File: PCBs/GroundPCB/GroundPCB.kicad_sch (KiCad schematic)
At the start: 42 parts, among them IC1 SWITCH-HSWA4-63DR+, IC2 SWITCH-HSWA4-63DR+, J1 SMA-LPRS-CONNECTOR, J2 Conn_02x03_Odd_Even, U1 HMC452ST89ETR, U2 PGA-103+, U3 RFM96W-433S2, U4 DS3231M

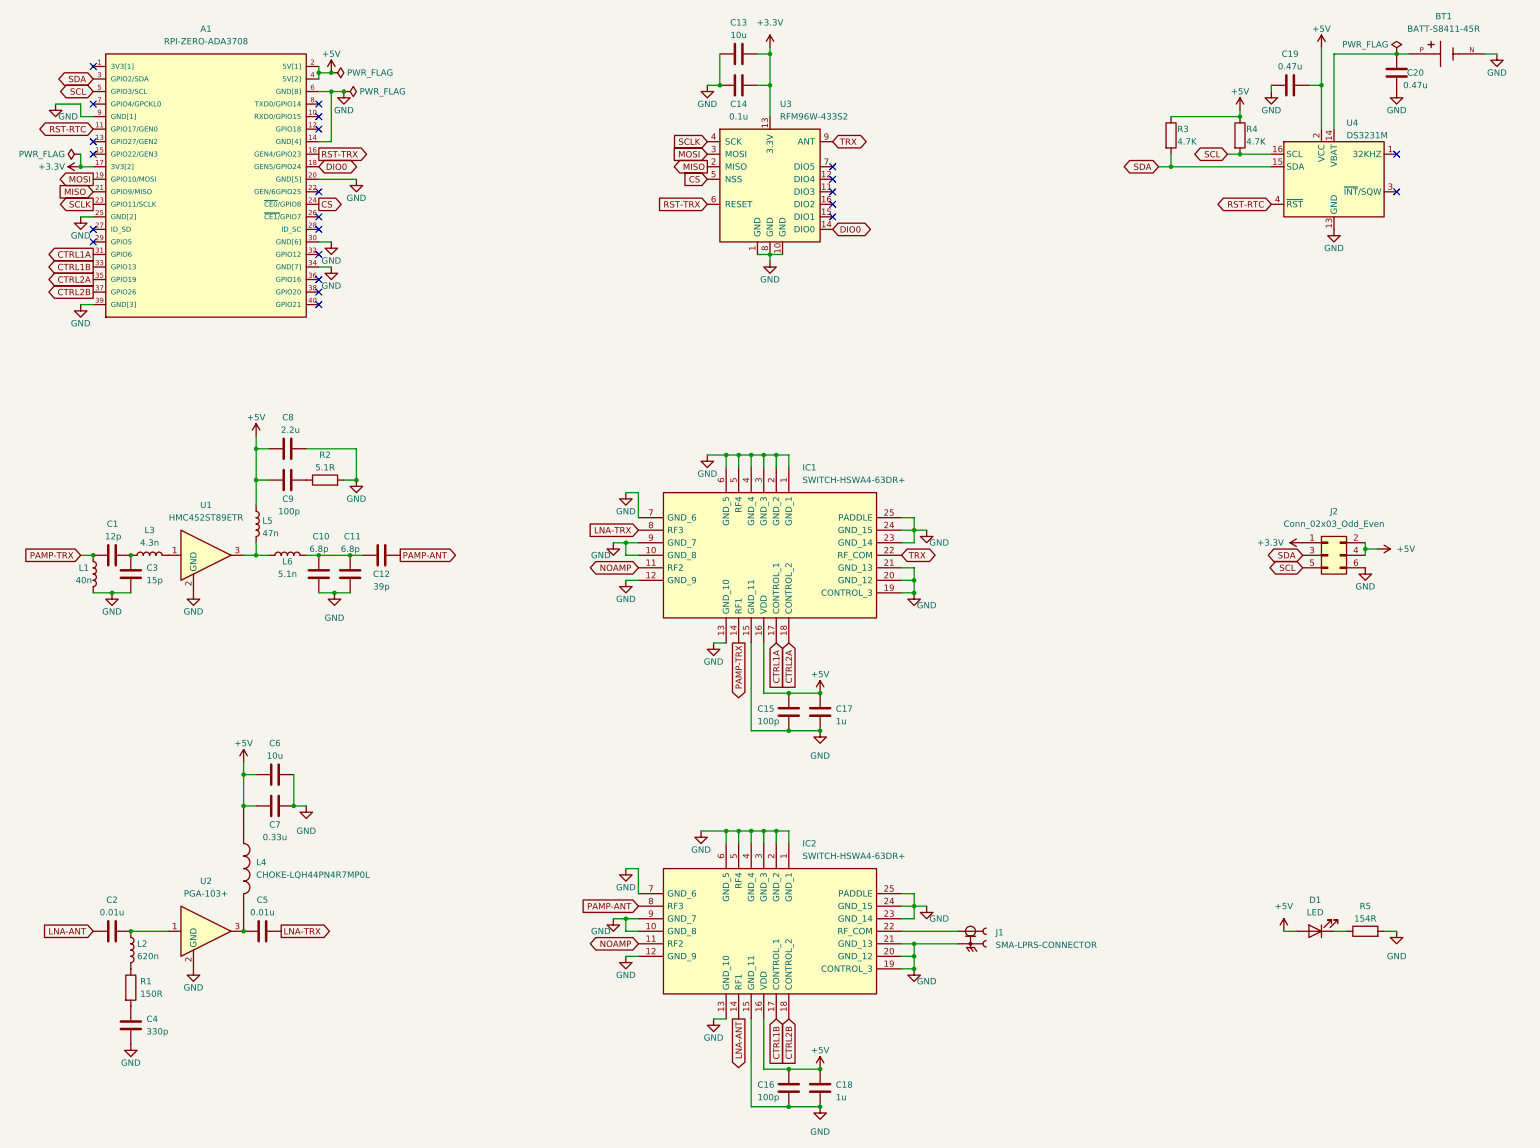
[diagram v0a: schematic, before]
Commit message: connectors, switch, test points
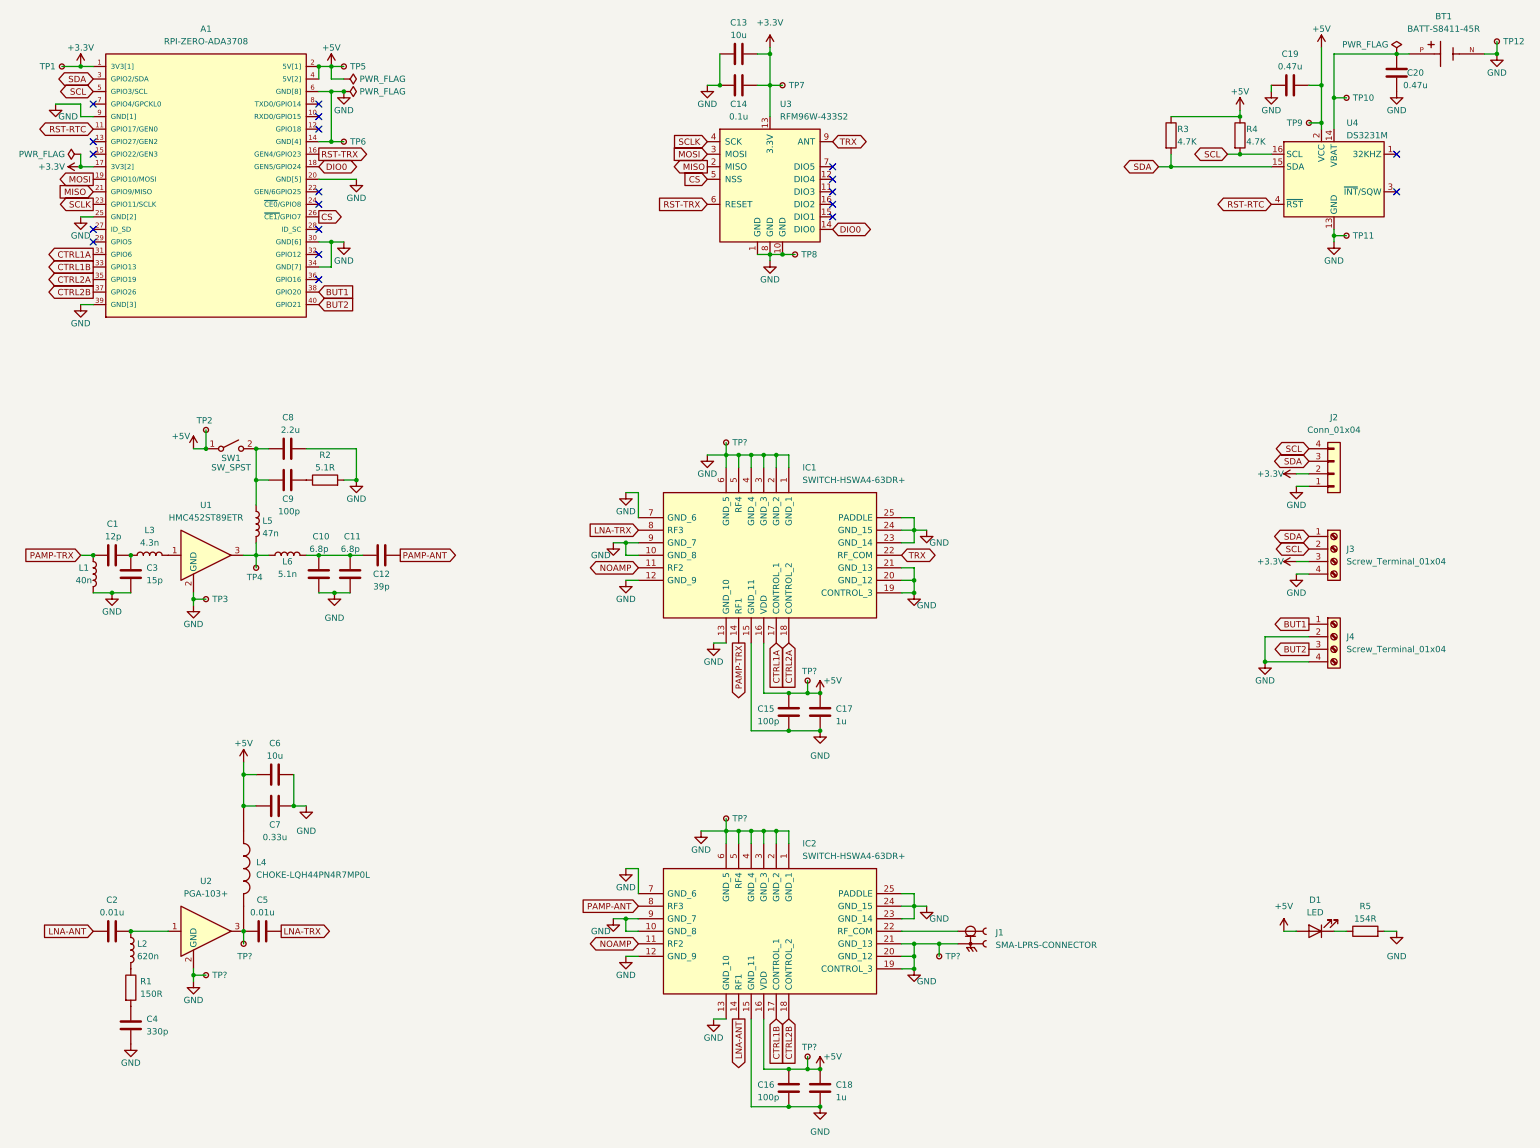
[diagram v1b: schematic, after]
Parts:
- removed J2: Conn_02x03_Odd_Even, Connector_PinHeader_2.54mm:PinHeader_2x03_P2.54mm_Vertical, symbol Connector_Generic:Conn_02x03_Odd_Even
- added J2: Conn_01x04, Connector_JST:JST_SH_SM04B-SRSS-TB_1x04-1MP_P1.00mm_Horizontal, symbol Connector_Generic:Conn_01x04
- added J3, J4: Screw_Terminal_01x04, TerminalBlock_Phoenix:TerminalBlock_Phoenix_MPT-0,5-4-2.54_1x04_P2.54mm_Horizontal, symbol Connector:Screw_Terminal_01x04
- added SW1: SW_SPST, Button_Switch_THT:SW_Push_2P1T_Toggle_CK_PVA1xxH1xxxxxxV2, symbol Switch:SW_SPST
- added TP1, TP10, TP11, TP12, TP2, TP3, TP4, TP5, TP6, TP7, TP8, TP9, TP? (x7): (no value), symbol Connector:TestPoint_Small
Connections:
- net +3.3V: now also A1.1 (3V3[1]), J2.2 (Pin_2), J3.3 (Pin_3), TP1.1, TP7.1
- net +5V: now also SW1.1 (A), TP2.1, TP5.1, TP9.1, TP?.1, TP?.1; no longer C8.1, C9.1, L5.1
- net CS: now also A1.26 (~{CE1/}GPIO7); no longer A1.24 (~{CE0}/GPIO8)
- net GND: now also J2.1 (Pin_1), J3.4 (Pin_4), J4.2 (Pin_2), J4.4 (Pin_4), TP11.1, TP12.1, TP3.1, TP6.1, TP8.1, TP?.1, TP?.1, TP?.1, TP?.1
- net SCL: now also J2.4 (Pin_4), J3.2 (Pin_2)
- net SDA: now also J2.3 (Pin_3), J3.1 (Pin_1)
- net at C5.1, L4.2, U2.3: now also TP?.1
- net at L5.2, L6.1, U1.3: now also TP4.1
- net at BT1.P, C20.1, U4.14 (VBAT): now also TP10.1
- net BUT1: now reaches A1.38 (GPIO20)
- net BUT1: now also J4.1 (Pin_1)
- net BUT2: now reaches A1.40 (GPIO21)
- net BUT2: now also J4.3 (Pin_3)
- new net: C8.1, C9.1, L5.1, SW1.2 (B)
- no-connect marks 23 -> 20

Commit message: initial layout changes
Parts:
- removed J3, J4: Screw_Terminal_01x04, TerminalBlock_Phoenix:TerminalBlock_Phoenix_MPT-0,5-4-2.54_1x04_P2.54mm_Horizontal, symbol Connector:Screw_Terminal_01x04
- added H1, H2, H3, H4: MountingHole, MountingHole:MountingHole_2.5mm, symbol Mechanical:MountingHole
- added J3: Conn_01x04, Connector_JST:JST_SH_SM04B-SRSS-TB_1x04-1MP_P1.00mm_Horizontal, symbol Connector_Generic:Conn_01x04
- TP1, TP2, TP3: footprint (none) -> TestPoint:TestPoint_Pad_D2.0mm
- TP10, TP13, TP14, TP15, TP4, TP5, TP9: renamed from TP?; footprint (none) -> TestPoint:TestPoint_Pad_D2.0mm
- TP11: renamed from TP7; footprint (none) -> TestPoint:TestPoint_Pad_D2.0mm
- TP12: renamed from TP8; footprint (none) -> TestPoint:TestPoint_Pad_D2.0mm
- TP16: renamed from TP9; footprint (none) -> TestPoint:TestPoint_Pad_D2.0mm
- TP17: renamed from TP10; footprint (none) -> TestPoint:TestPoint_Pad_D2.0mm
- TP18: renamed from TP11; footprint (none) -> TestPoint:TestPoint_Pad_D2.0mm
- TP19: renamed from TP12; footprint (none) -> TestPoint:TestPoint_Pad_D2.0mm
- TP6: renamed from TP4; footprint (none) -> TestPoint:TestPoint_Pad_D2.0mm
- TP7: renamed from TP5; footprint (none) -> TestPoint:TestPoint_Pad_D2.0mm
- TP8: renamed from TP6; footprint (none) -> TestPoint:TestPoint_Pad_D2.0mm
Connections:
- net +5V: now also SW1.3 (A)
- net BUT1: now also A1.36 (GPIO16), J3.4 (Pin_4); no longer A1.38 (GPIO20)
- net BUT2: now also A1.38 (GPIO20), J3.3 (Pin_3); no longer A1.40 (GPIO21)
- net GND: now also J3.1 (Pin_1)
- net at C8.1, C9.1, L5.1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: now also SW1.4 (B)
- new net BUT3: A1.40 (GPIO21), J3.2 (Pin_2)
- no-connect marks 20 -> 21
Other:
- title: RF Communications Ground PCB -> NARWAL
- moved on the sheet: D1, R5

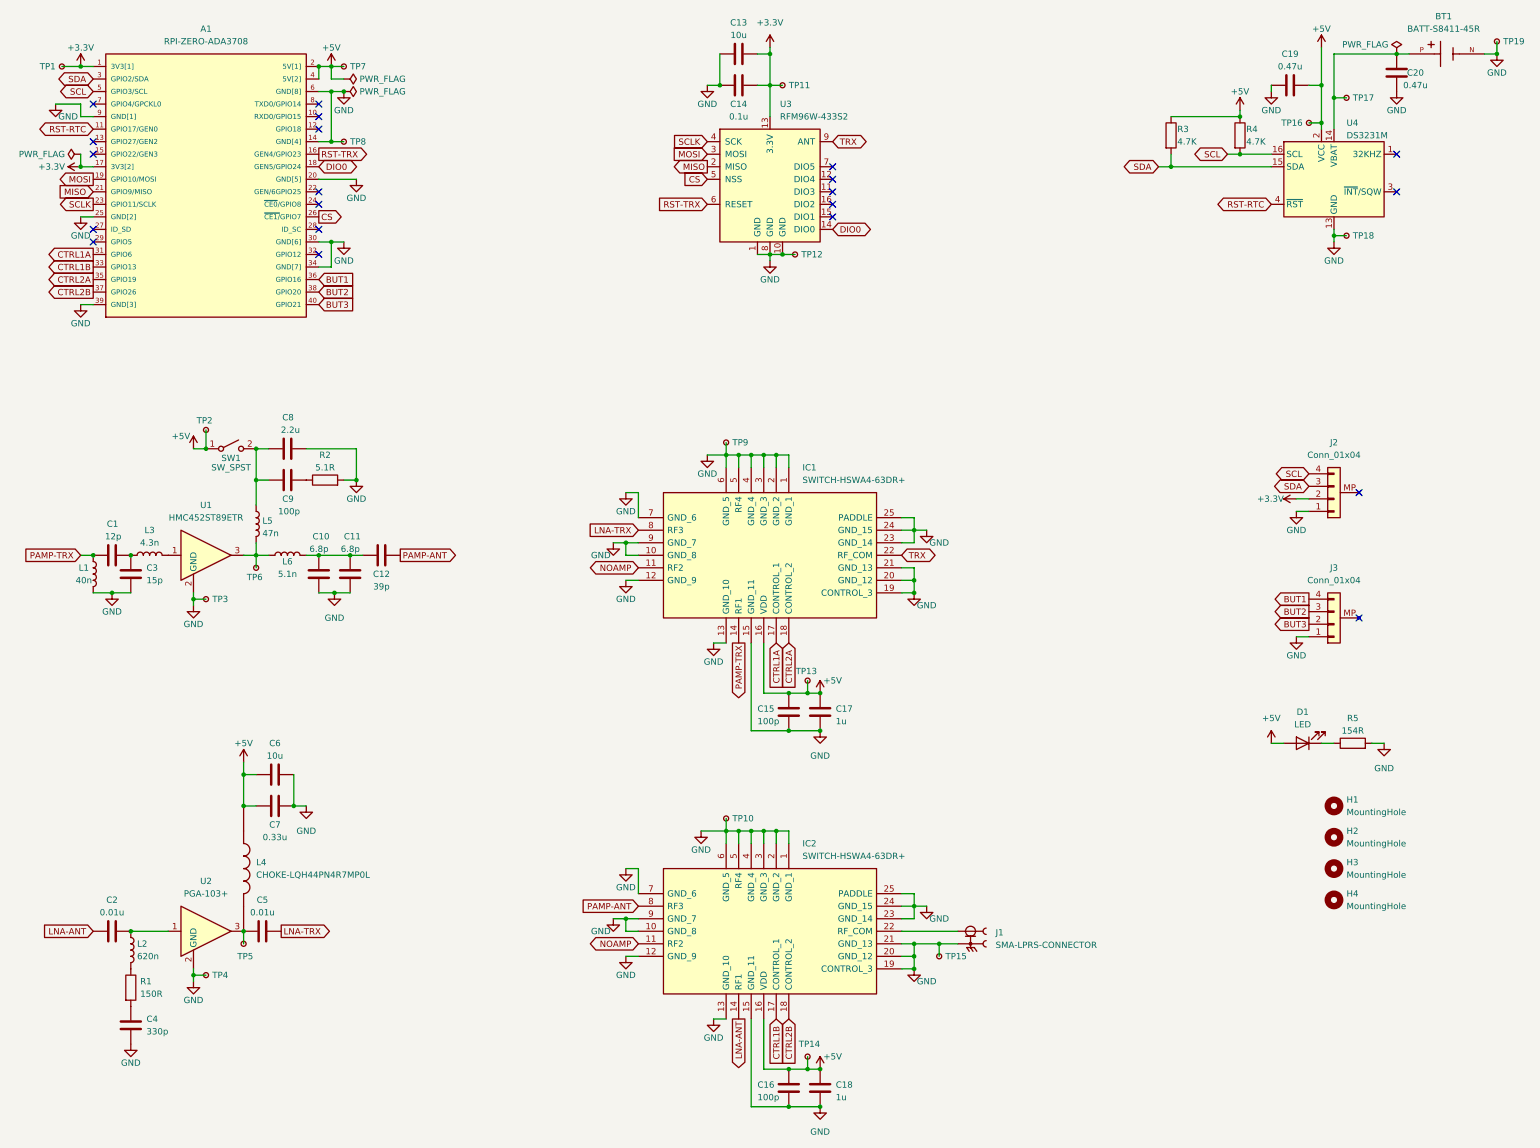
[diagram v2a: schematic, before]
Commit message: relocated components, added switch to layout
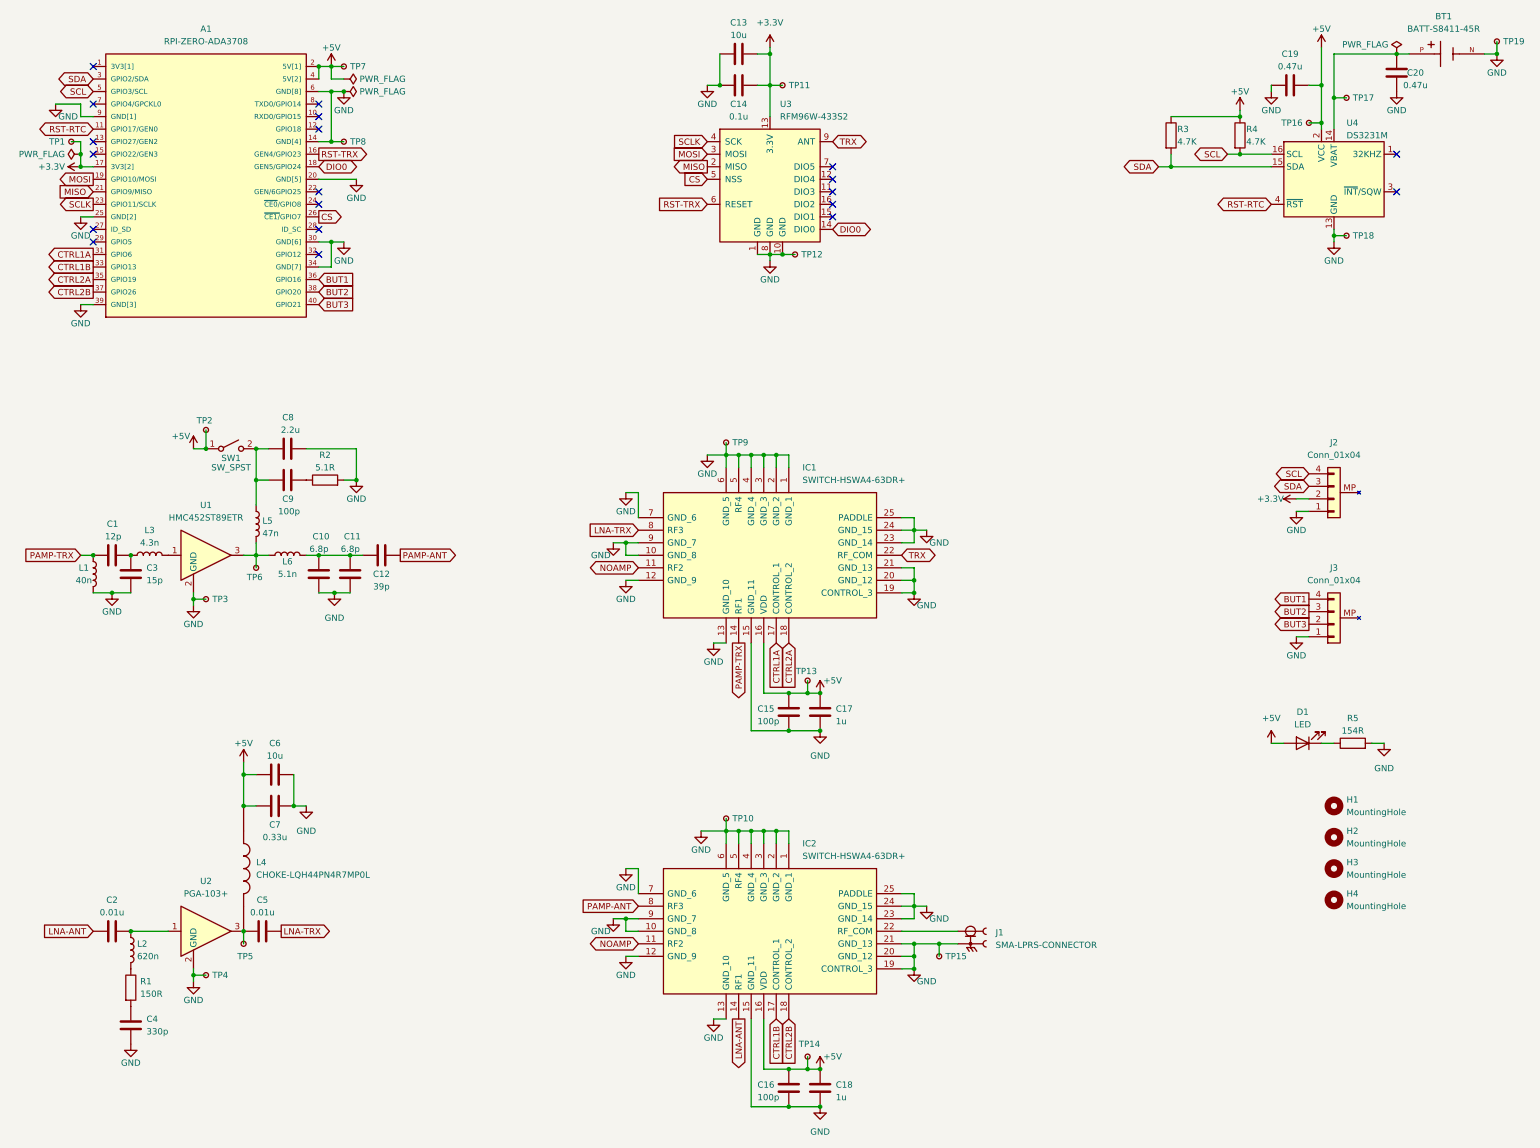
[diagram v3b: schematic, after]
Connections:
- net +3.3V: no longer A1.1 (3V3[1])
- no-connect marks 21 -> 20
